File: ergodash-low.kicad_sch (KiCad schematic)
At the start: 78 parts, among them J1 Conn_01x02, J2 AudioJack4, SW1 SW_Push, SW10 SW_Push, SW11 SW_Push, SW12 SW_Push, SW13 SW_Push, SW14 SW_Push, SW15 SW_Push, SW16 SW_Push, SW17 SW_Push, SW18 SW_Push, SW19 SW_Push, SW2 SW_Push, SW20 SW_Push, SW21 SW_Push, SW22 SW_Push, SW23 SW_Push, SW24 SW_Push, SW25 SW_Push, SW26 SW_Push, SW27 SW_Push, SW28 SW_Push, SW29 SW_Push, SW3 SW_Push, SW30 SW_Push, SW31 SW_Push, SW32 SW_Push, SW33 SW_Push, SW4 SW_Push, SW5 SW_Push, SW6 SW_Push, SW7 SW_Push, SW8 SW_Push, SW9 SW_Push, U1 ProMicro, U2 ProMicro

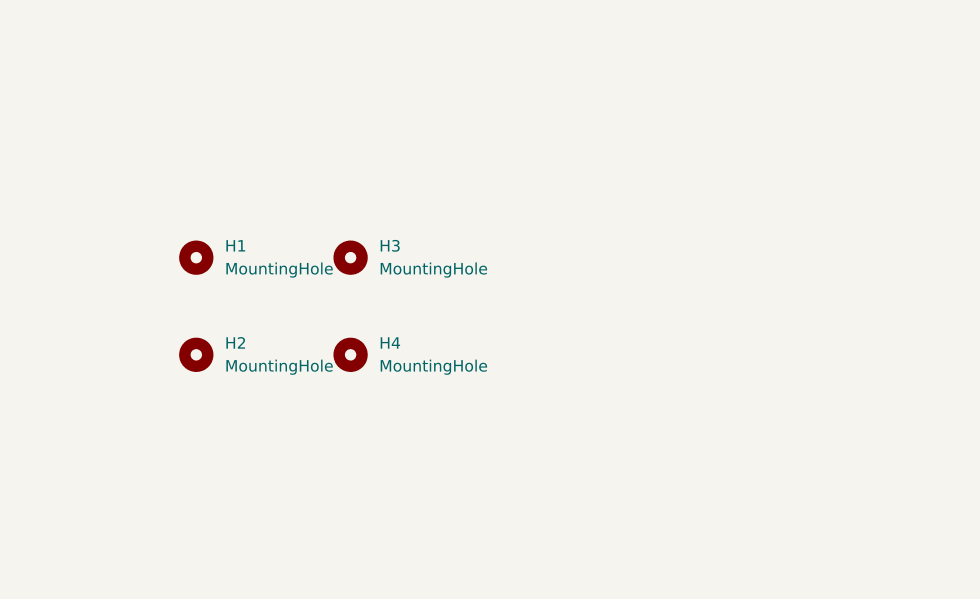
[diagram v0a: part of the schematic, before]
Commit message: completed schematic and pcb
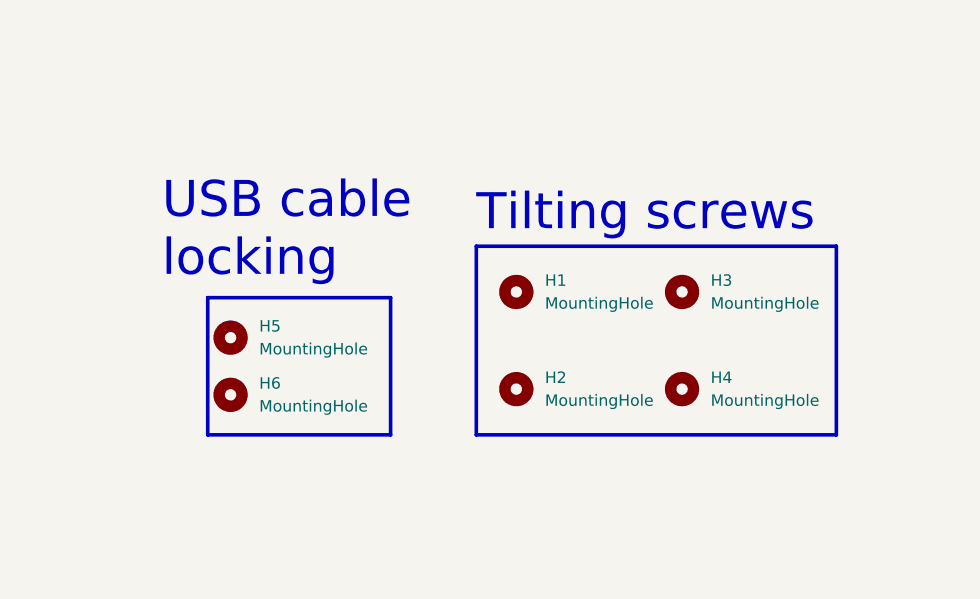
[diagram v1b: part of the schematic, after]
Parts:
- added H5, H6: MountingHole, MountingHole:MountingHole_4mm, symbol Mechanical:MountingHole
- D1, D10, D11, D12, D13, D14, D15, D16, D17, D18, D19, D2, D20, D21, D22, D23, D24, D25, D26, D27, D28, D29, D3, D30, D31, D32, D33, D4, D5, D6, D7, D8, D9: footprint local-lib:D_0603_1608Metric_Pad1.05x0.95mm_HandSolder -> local-lib:D_SOD-123-reversible
- H1, H2, H3, H4: footprint MountingHole:MountingHole_3.2mm_M3 -> MountingHole:MountingHole_5.3mm_M5
- J2: footprint Connector_Audio:Jack_3.5mm_PJ320D_Horizontal -> local-lib:TRRS-PJ-320A-dual
- SW1, SW10, SW11, SW12, SW13, SW14, SW15, SW16, SW17, SW18, SW19, SW20, SW21, SW22, SW23, SW24, SW25, SW26, SW27, SW28, SW3, SW30, SW31, SW32, SW4, SW5, SW6, SW7, SW8, SW9: footprint local-lib:SW_MX_reversible -> local-lib:gateron_ks27_reversible
- SW2, SW29, SW33: footprint local-lib:SW_MX_reversible_2u_stab -> local-lib:gateron_ks27_reversible_stabilizer
- U1, U2: footprint local-lib:ProMicro-EnforcedTop -> local-lib:ProMicro
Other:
- note added: "Tilting screws"
- note added: "USB cable locking"
- moved on the sheet: H1, H2, H3, H4
